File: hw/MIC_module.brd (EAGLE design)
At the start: 25 x 45 mm, 42 parts, among them IC1 STM32F405RGT, J1 GROVE-4P-2.0-3470130P1, J2 GROVE-4P-2.0-3470130P1, J4 MICRO-USB-5P-340015001

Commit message: layout completed
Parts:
- removed R3: 10k, rcl:R0603
- added C19: 100n, rcl:C0603
- added X1: 53047-04, con-molex:53047-04
- added X2: 53047-06, con-molex:53047-06
- moved R1 10.4 mm to (15.9, 7.70)
- moved C17 9.35 mm to (22.7, 21.5), turned to 0 degrees
- moved R5 7.17 mm to (12.4, 29.5)
- moved C3 5.00 mm to (5.50, 15.1)
- moved C15 4.32 mm to (13.9, 29.5)
- moved R8 3.45 mm to (7.40, 28.7), turned to 180 degrees
- moved R6 3.00 mm to (7.40, 30.2), turned to 180 degrees
- moved C14 1.02 mm to (9.60, 29.5)
- moved C18 1.00 mm to (11.0, 29.5)
- moved R2 0.86 mm to (13.8, 33.5), turned to 270 degrees
- moved R4 0.86 mm to (11.2, 33.5), turned to 270 degrees
- moved C10 0.50 mm to (6.00, 42.0)
- moved C11 0.50 mm to (19.0, 42.0)
- moved C12 0.50 mm to (6.00, 38.0)
- moved C13 0.50 mm to (19.0, 38.0)
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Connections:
- removed net BOOT0: IC1.60, R3.2
- new net I2C2_SCL: IC1.29, X1.3
- new net I2C2_SDA: IC1.30, X1.4
- new net I2S3_CK: IC1.51, X2.4
- new net I2S3_MCK: IC1.38, X2.5
- new net I2S3_SD: IC1.53, X2.3
- new net I2S3_WS: IC1.20, X2.6
- new net MIC_CLK_X2: IC1.21, IC1.22, IC1.34
- net +3V3: now also C19.1, X1.1, X2.1
- net GND: now also C19.2, IC1.60, LED1.C, X1.2, X2.2; no longer LED1.A, R3.1
- net LED1: now also IC1.59
- net MIC_CLK_UC: now also IC1.26
- net MIC_PDM12: now also IC1.36
- net MIC_PDM34: now also IC1.23
- net N$4: now also LED1.A; no longer LED1.C
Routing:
- net I2S3_CK: track 0.00 -> 25.7 mm, vias 0 -> 1
- net I2S3_SD: track 0.00 -> 24.0 mm, vias 0 -> 1
- net +3V3: track 137.5 -> 158.6 mm, vias 12 -> 13
- net I2S3_MCK: track 0.00 -> 20.3 mm, vias 0 -> 1
- net N$4: track 17.9 -> 4.55 mm, vias 2 -> 0
- net I2C2_SCL: track 0.00 -> 11.1 mm, vias 0 -> 1
- net I2C2_SDA: track 0.00 -> 10.8 mm, vias 0 -> 1
- net MIC_CLK_X2: track 0.00 -> 9.12 mm
- net MIC_PDM34: track 36.3 -> 44.7 mm, vias 2 -> 3
- net LED1: track 0.00 -> 5.65 mm
- net BOOT0: track 5.44 -> 0.00 mm
- net I2S3_WS: track 0.00 -> 5.37 mm
- net MIC_CLK_UC: track 1.34 -> 3.57 mm
- net N$32: track 14.3 -> 12.6 mm
- net MIC_PDM12: track 37.1 -> 38.6 mm, vias 2 -> 3
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
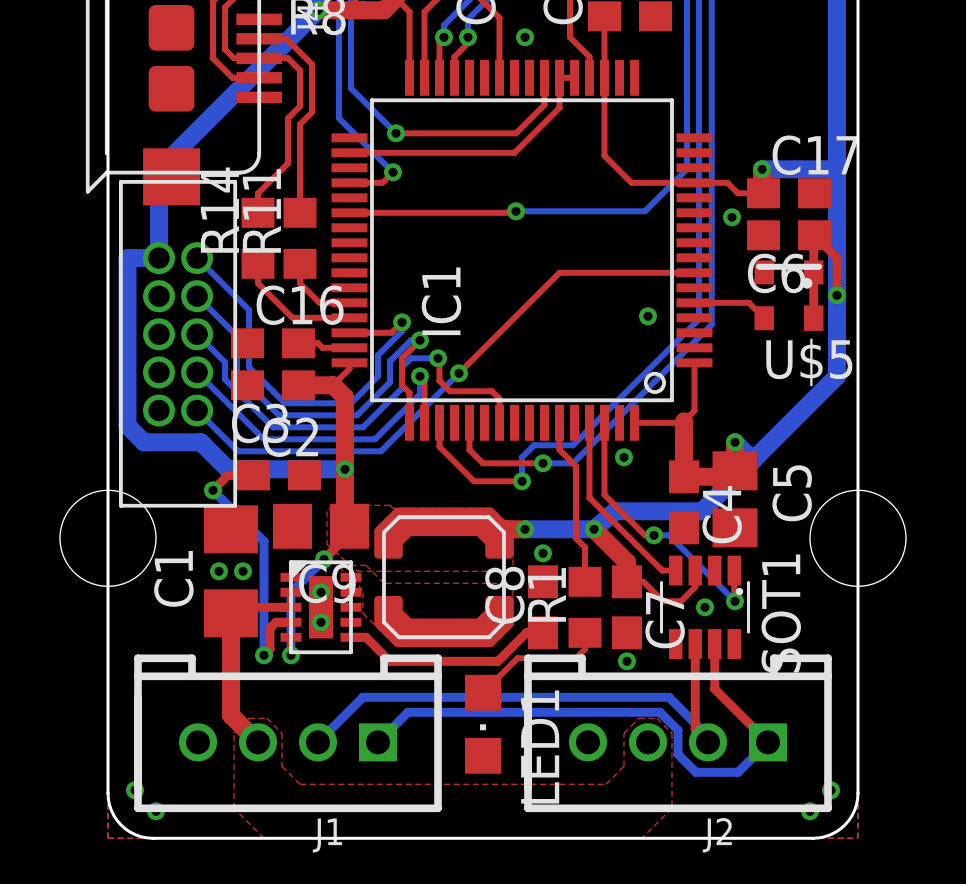
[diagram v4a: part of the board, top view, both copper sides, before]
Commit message: Fixed silkscreen
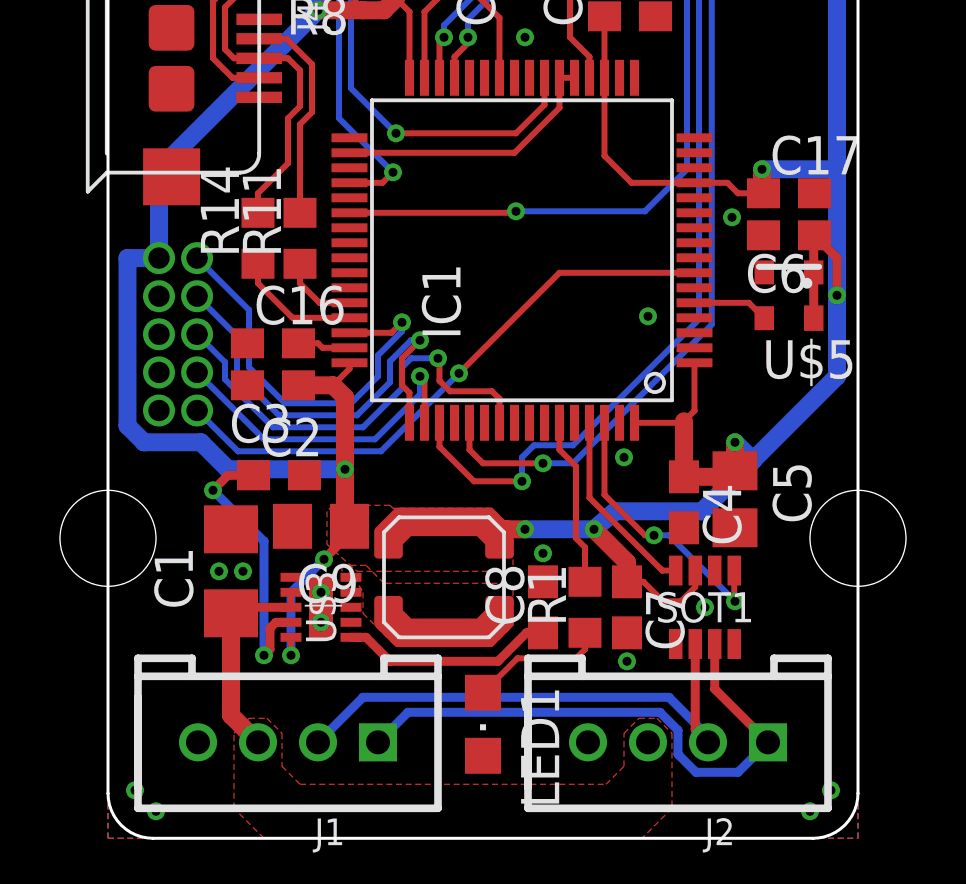
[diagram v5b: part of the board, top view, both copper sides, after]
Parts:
- SOT1: device maxim:SOT23-8L -> r2p_ic:SOT23-8L
- U$3: device maxim:TDFN-10 -> r2p_ic:TDFN-10
- U$4: value FTSH-105TH -> JTAG-TH; device samtec:FTSH-105-TH -> r2p_connector:SAMTEC_FTSH-105-TH
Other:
- board text added: "I2C"
- board text added: "I2S"
- board text added: "MIC module v1.0 (2015/02)"
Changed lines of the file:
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@@
 <wire x1="6.55" y1="8" x2="6.55" y2="8.8" width="0.2" layer="41"/>
 <wire x1="6.55" y1="8.8" x2="7.45" y2="8.8" width="0.2" layer="41"/>
+<text x="4" y="6" size="1.5" layer="200" rot="MR90">MIC module
+v1.0 (2015/02)</text>
+<text x="23.1" y="27.7" size="1" layer="48" font="vector" align="top-center">I2S</text>
+<text x="20.6" y="36.4" size="1" layer="48" font="vector" align="top-center">I2C</text>
 </plain>
 <attributes>
@@
 <element name="LED1" library="led" package="CHIPLED_0805" value="" x="12.5" y="3.8" rot="R180"/>
 <element name="R1" library="rcl" package="R0603" value="330" x="15.9" y="7.7" rot="R90"/>
-<element name="U$4" library="samtec" package="FTSH-105-TH" value="FTSH-105TH" x="1.7" y="16.8" rot="R270"/>
+<element name="U$4" library="r2p_connector" package="SAMTEC_FTSH-105-TH" value="JTAG-TH" x="1.7" y="16.8" rot="R270"/>
 <element name="J2" library="OPL Eagle Library" package="4P-2.0" value="GROVE-4P-2.0-3470130P1" x="19" y="3.2" rot="R180"/>
 <element name="U$2" library="coilcraft" package="LPS4018" value="LPS4018" x="11.2" y="8.7" rot="R90"/>
@@
 <element name="C8" library="rcl" package="C0603" value="10n" x="14.5" y="7.7" rot="R90"/>
 <element name="C9" library="rcl" package="C0805" value="" x="7.1" y="10.4" rot="R180"/>
-<element name="U$3" library="maxim" package="TDFN-10" value="MAX17501" x="7.1" y="7.7"/>
+<element name="U$3" library="r2p_ic" package="TDFN-10" value="MAX17501" x="7.1" y="7.7"/>
 <element name="J1" library="OPL Eagle Library" package="4P-2.0" value="GROVE-4P-2.0-3470130P1" x="6" y="3.2" rot="R180"/>
-<element name="SOT1" library="maxim" package="SOT23-8L" value="MAX3051EKA" x="19.9" y="7.7" rot="R180"/>
+<element name="SOT1" library="r2p_ic" package="SOT23-8L" value="MAX3051EKA" x="19.9" y="7.7" rot="R180"/>
 <element name="U$1" library="r2p_pcb" package="25X45" value="PCB_25X45" x="0" y="0"/>
 <element name="U$5" library="abracon" package="2.5X2" value="ASD" x="22.7" y="18.1" rot="R180"/>
@@
 </board>
 </drawing>
+<compatibility>
+<note version="6.3" minversion="6.2.2" severity="warning">
+Since Version 6.2.2 text objects can contain more than one line,
+which will not be processed correctly with this version.
+</note>
+</compatibility>
 </eagle>
